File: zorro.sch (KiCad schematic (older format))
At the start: 76 parts, among them CN601 zorro_socket, CN602 zorro_socket, CN603 zorro_socket, CN604 zorro_socket, CN605 zorro_socket, CN606 Conn_01x04_Male, J1 Conn_01x03_Male, J2 Conn_01x03_Male, U606 74LS32

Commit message: Rename bus with correct syntax
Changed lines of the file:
@@
-EESchema Schematic File Version 4
+EESchema Schematic File Version 5
 LIBS:amiga2000-cache
 EELAYER 29 0
@@
 	14150 14500 14250 14600
 Text GLabel 4950 14600 0    50   Input ~ 0
-_SLAVE(1:5)
+_SLAVE[1..5]
 Wire Wire Line
 	7350 4200 9350 4200
@@
 	4650 5000 4150 5000
 Text GLabel 4150 5000 0    50   Input ~ 0
-BA(1:23)
+BA[1..23]
 Text Label 7400 9200 0    50   ~ 0
 _BR1
@@
 _BG5
 Text GLabel 4950 14450 0    50   Input ~ 0
-_EBR(1:5)
+_EBR[1..5]
 Text GLabel 4950 14300 0    50   Input ~ 0
-_EBG(1:5)
+_EBG[1..5]
 Wire Wire Line
 	7350 9600 7450 9600
@@
 	4600 9400 3950 9400
 Text GLabel 3950 9400 0    50   Input ~ 0
-BD(0:15)
+BD[0..15]
 $Comp
 L Device:C_Small C654
@@
 _IPL0
 Text GLabel 3050 6700 0    50   Input ~ 0
-_IPL(0:2)
+_IPL[0..2]
 $Comp
 L Device:R_Network09 RP601

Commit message: Some ERC things
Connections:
- net OVR renamed _OVR
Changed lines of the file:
@@
-EESchema Schematic File Version 5
+EESchema Schematic File Version 4
 LIBS:amiga2000-cache
 EELAYER 29 0
@@
 Connection ~ 15600 4800
 Text GLabel 6200 4900 0    50   Input ~ 0
-OVR
+_OVR
 Wire Wire Line
 	6200 4900 6300 4900

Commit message: Rename some bus things
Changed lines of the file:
@@
 _BG5
 Text GLabel 4950 14450 0    50   Input ~ 0
-_EBR[1..5]
+_BR[1..5]
 Text GLabel 4950 14300 0    50   Input ~ 0
-_EBG[1..5]
+_BG[1..5]
 Wire Wire Line
 	7350 9600 7450 9600

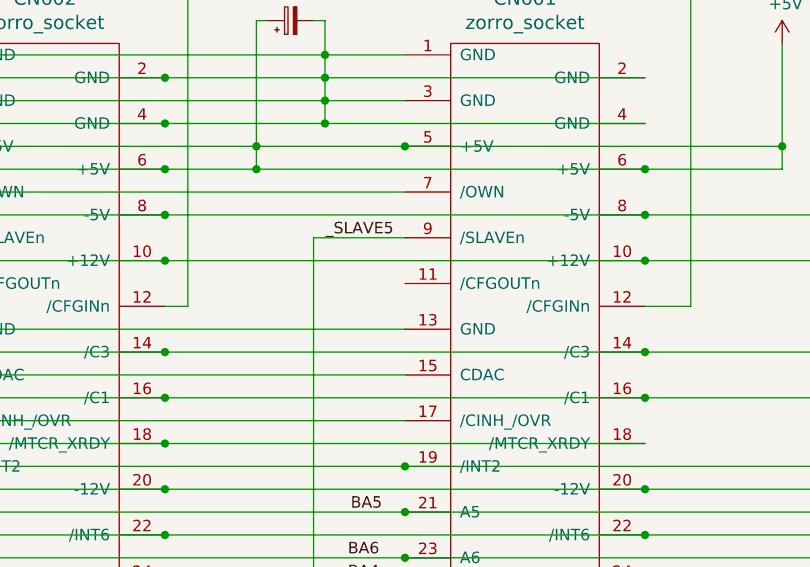
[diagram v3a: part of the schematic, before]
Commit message: Fix a bunch of DRC errors
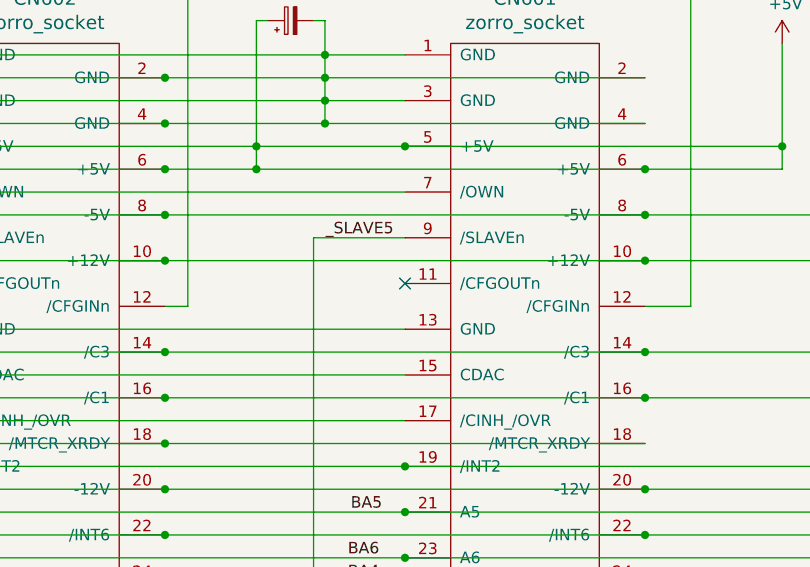
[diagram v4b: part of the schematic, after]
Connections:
- no-connect marks 0 -> 1
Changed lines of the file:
@@
 	0    -1   -1   0
 $EndComp
+NoConn ~ 14550 4300
 Wire Bus Line
 	3350 6700 3350 7050

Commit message: One more review
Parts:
- added RP600: 10k, Resistor_THT:R_Array_SIP8, symbol Device:R_Network07
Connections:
- net +5V: now also RP600.1 (common)
- net _BR1: now also RP600.6 (R5)
- net _BR2: now also RP600.5 (R4)
- net _BR3: now also RP600.4 (R3)
- net _BR4: now also RP600.3 (R2)
- net _BR5: now also RP600.2 (R1)
- no-connect marks 1 -> 3
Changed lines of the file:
@@
 $EndComp
 NoConn ~ 14550 4300
+$Comp
+L Device:R_Network07 RP600
+U 1 1 5D083E80
+P 17000 14950
+F 0 "RP600" V 16483 14950 50  0000 C CNN
+F 1 "10k" V 16574 14950 50  0000 C CNN
+F 2 "Resistor_THT:R_Array_SIP8" V 17475 14950 50  0001 C CNN
+F 3 "http://www.vishay.com/docs/31509/csc.pdf" H 17000 14950 50  0001 C CNN
+	1    17000 14950
+	0    1    1    0
+$EndComp
+Text Label 16550 14650 0    50   ~ 0
+_BR5
+Text Label 16550 14750 0    50   ~ 0
+_BR4
+Text Label 16550 14850 0    50   ~ 0
+_BR3
+Text Label 16550 14950 0    50   ~ 0
+_BR2
+Text Label 16550 15050 0    50   ~ 0
+_BR1
+$Comp
+L power:+5V #PWR0270
+U 1 1 5D186BDE
+P 17200 14650
+F 0 "#PWR0270" H 17200 14500 50  0001 C CNN
+F 1 "+5V" H 17215 14823 50  0000 C CNN
+F 2 "" H 17200 14650 50  0001 C CNN
+F 3 "" H 17200 14650 50  0001 C CNN
+	1    17200 14650
+	0    1    1    0
+$EndComp
+NoConn ~ 16800 15150
+NoConn ~ 16800 15250
+Entry Wire Line
+	16350 14550 16450 14650
+Entry Wire Line
+	16350 14650 16450 14750
+Entry Wire Line
+	16350 14750 16450 14850
+Entry Wire Line
+	16350 14850 16450 14950
+Entry Wire Line
+	16350 14950 16450 15050
+Wire Wire Line
+	16450 14650 16800 14650
+Wire Wire Line
+	16450 14750 16800 14750
+Wire Wire Line
+	16450 14850 16800 14850
+Wire Wire Line
+	16450 14950 16800 14950
+Wire Wire Line
+	16450 15050 16800 15050
 Wire Bus Line
 	3350 6700 3350 7050
-Wire Bus Line
-	4950 14450 16000 14450
 Wire Bus Line
 	4950 14600 14250 14600
@@
 	4950 14300 15850 14300
 Wire Bus Line
+	4950 14450 16350 14450
+Wire Bus Line
+	16350 14450 16350 14950
+Wire Bus Line
 	4600 9400 4600 11700

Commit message: Associate footprints with components
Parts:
- CN606: footprint (none) -> Connector_PinSocket_2.54mm:PinSocket_1x04_P2.54mm_Vertical
- J1, J2: footprint (none) -> Connector_PinSocket_2.54mm:PinSocket_1x03_P2.54mm_Vertical
- R311, R312, R601, R603, R604, R605, R901: footprint (none) -> Resistor_THT:R_Axial_DIN0207_L6.3mm_D2.5mm_P10.16mm_Horizontal
- U606: footprint (none) -> Package_DIP:DIP-14_W7.62mm_Socket
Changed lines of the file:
@@
 F 0 "CN604" H 8825 3447 60  0000 C CNN
 F 1 "zorro_socket" H 8825 3341 60  0000 C CNN
-F 2 "" H 8300 950 60  0000 C CNN
+F 2 "" H 8300 950 60  0001 C CNN
 F 3 "" H 8300 950 60  0000 C CNN
 	1    8800 3250
@@
 F 0 "CN603" H 11025 3447 60  0000 C CNN
 F 1 "zorro_socket" H 11025 3341 60  0000 C CNN
-F 2 "" H 10500 950 60  0000 C CNN
+F 2 "" H 10500 950 60  0001 C CNN
 F 3 "" H 10500 950 60  0000 C CNN
 	1    11000 3250
@@
 F 0 "CN602" H 12975 3447 60  0000 C CNN
 F 1 "zorro_socket" H 12975 3341 60  0000 C CNN
-F 2 "" H 12450 950 60  0000 C CNN
+F 2 "" H 12450 950 60  0001 C CNN
 F 3 "" H 12450 950 60  0000 C CNN
 	1    12950 3250
@@
 F 0 "CN601" H 15075 3447 60  0000 C CNN
 F 1 "zorro_socket" H 15075 3341 60  0000 C CNN
-F 2 "" H 14550 950 60  0000 C CNN
+F 2 "" H 14550 950 60  0001 C CNN
 F 3 "" H 14550 950 60  0000 C CNN
 	1    15050 3250
@@
 F 0 "CN605" H 6825 3447 60  0000 C CNN
 F 1 "zorro_socket" H 6825 3341 60  0000 C CNN
-F 2 "" H 6300 950 60  0000 C CNN
+F 2 "" H 6300 950 60  0001 C CNN
 F 3 "" H 6300 950 60  0000 C CNN
 	1    6800 3250
@@
 F 0 "R312" H 17320 3446 50  0000 L CNN
 F 1 "1k" H 17320 3355 50  0000 L CNN
-F 2 "" V 17180 3400 50  0001 C CNN
+F 2 "Resistor_THT:R_Axial_DIN0207_L6.3mm_D2.5mm_P10.16mm_Horizontal" V 17180 3400 50  0001 C CNN
 F 3 "~" H 17250 3400 50  0001 C CNN
 	1    17250 3400
@@
 F 0 "R311" H 17670 3446 50  0000 L CNN
 F 1 "1k" H 17670 3355 50  0000 L CNN
-F 2 "" V 17530 3400 50  0001 C CNN
+F 2 "Resistor_THT:R_Axial_DIN0207_L6.3mm_D2.5mm_P10.16mm_Horizontal" V 17530 3400 50  0001 C CNN
 F 3 "~" H 17600 3400 50  0001 C CNN
 	1    17600 3400
@@
 F 0 "U606" H 7800 2625 50  0000 C CNN
 F 1 "74LS32" H 7800 2534 50  0000 C CNN
-F 2 "" H 7800 2300 50  0001 C CNN
+F 2 "Package_DIP:DIP-14_W7.62mm_Socket" H 7800 2300 50  0001 C CNN
 F 3 "http://www.ti.com/lit/gpn/sn74LS32" H 7800 2300 50  0001 C CNN
 	4    7800 2300
@@
 F 0 "U606" H 9900 2725 50  0000 C CNN
 F 1 "74LS32" H 9900 2634 50  0000 C CNN
-F 2 "" H 9900 2400 50  0001 C CNN
+F 2 "Package_DIP:DIP-14_W7.62mm_Socket" H 9900 2400 50  0001 C CNN
 F 3 "http://www.ti.com/lit/gpn/sn74LS32" H 9900 2400 50  0001 C CNN
 	1    9900 2400
@@
 F 0 "U606" H 12100 2825 50  0000 C CNN
 F 1 "74LS32" H 12100 2734 50  0000 C CNN
-F 2 "" H 12100 2500 50  0001 C CNN
+F 2 "Package_DIP:DIP-14_W7.62mm_Socket" H 12100 2500 50  0001 C CNN
 F 3 "http://www.ti.com/lit/gpn/sn74LS32" H 12100 2500 50  0001 C CNN
 	2    12100 2500
@@
 F 0 "U606" H 14000 2925 50  0000 C CNN
 F 1 "74LS32" H 14000 2834 50  0000 C CNN
-F 2 "" H 14000 2600 50  0001 C CNN
+F 2 "Package_DIP:DIP-14_W7.62mm_Socket" H 14000 2600 50  0001 C CNN
 F 3 "http://www.ti.com/lit/gpn/sn74LS32" H 14000 2600 50  0001 C CNN
 	3    14000 2600
@@
 F 0 "J1" V 16800 13250 50  0000 R CNN
 F 1 "Conn_01x03_Male" V 16963 13012 50  0001 R CNN
-F 2 "" H 16900 13200 50  0001 C CNN
+F 2 "Connector_PinSocket_2.54mm:PinSocket_1x03_P2.54mm_Vertical" H 16900 13200 50  0001 C CNN
 F 3 "~" H 16900 13200 50  0001 C CNN
 	1    16900 13200
@@
 F 0 "J2" V 17150 13150 50  0000 R CNN
 F 1 "Conn_01x03_Male" V 17313 12912 50  0001 R CNN
-F 2 "" H 17250 13100 50  0001 C CNN
+F 2 "Connector_PinSocket_2.54mm:PinSocket_1x03_P2.54mm_Vertical" H 17250 13100 50  0001 C CNN
 F 3 "~" H 17250 13100 50  0001 C CNN
 	1    17250 13100
@@
 F 0 "U606" H 19730 14196 50  0000 L CNN
 F 1 "74LS32" H 19730 14105 50  0000 L CNN
-F 2 "" H 19500 14150 50  0001 C CNN
+F 2 "Package_DIP:DIP-14_W7.62mm_Socket" H 19500 14150 50  0001 C CNN
 F 3 "http://www.ti.com/lit/gpn/sn74LS32" H 19500 14150 50  0001 C CNN
 	5    19500 14150
@@
 F 0 "R603" H 18130 12854 50  0000 R CNN
 F 1 "1k" H 18130 12945 50  0000 R CNN
-F 2 "" V 18130 12900 50  0001 C CNN
+F 2 "Resistor_THT:R_Axial_DIN0207_L6.3mm_D2.5mm_P10.16mm_Horizontal" V 18130 12900 50  0001 C CNN
 F 3 "~" H 18200 12900 50  0001 C CNN
 	1    18200 12900
@@
 F 0 "R601" H 18580 12854 50  0000 R CNN
 F 1 "1k" H 18580 12945 50  0000 R CNN
-F 2 "" V 18580 12900 50  0001 C CNN
+F 2 "Resistor_THT:R_Axial_DIN0207_L6.3mm_D2.5mm_P10.16mm_Horizontal" V 18580 12900 50  0001 C CNN
 F 3 "~" H 18650 12900 50  0001 C CNN
 	1    18650 12900
@@
 F 0 "R605" H 21280 11104 50  0000 R CNN
 F 1 "1k" H 21280 11195 50  0000 R CNN
-F 2 "" V 21280 11150 50  0001 C CNN
+F 2 "Resistor_THT:R_Axial_DIN0207_L6.3mm_D2.5mm_P10.16mm_Horizontal" V 21280 11150 50  0001 C CNN
 F 3 "~" H 21350 11150 50  0001 C CNN
 	1    21350 11150
@@
 F 0 "R604" H 21730 11104 50  0000 R CNN
 F 1 "1k" H 21730 11195 50  0000 R CNN
-F 2 "" V 21730 11150 50  0001 C CNN
+F 2 "Resistor_THT:R_Axial_DIN0207_L6.3mm_D2.5mm_P10.16mm_Horizontal" V 21730 11150 50  0001 C CNN
 F 3 "~" H 21800 11150 50  0001 C CNN
 	1    21800 11150
@@
 F 0 "R901" H 21820 5296 50  0000 L CNN
 F 1 "Xk" H 21820 5205 50  0000 L CNN
-F 2 "" V 21680 5250 50  0001 C CNN
+F 2 "Resistor_THT:R_Axial_DIN0207_L6.3mm_D2.5mm_P10.16mm_Horizontal" V 21680 5250 50  0001 C CNN
 F 3 "~" H 21750 5250 50  0001 C CNN
 	1    21750 5250
@@
 F 0 "CN606" H 3922 6978 50  0000 R CNN
 F 1 "Conn_01x04_Male" H 4058 7240 50  0001 C CNN
-F 2 "" H 3950 7050 50  0001 C CNN
+F 2 "Connector_PinSocket_2.54mm:PinSocket_1x04_P2.54mm_Vertical" H 3950 7050 50  0001 C CNN
 F 3 "~" H 3950 7050 50  0001 C CNN
 	1    3950 7050
@@
 	4950 14300 15850 14300
 Wire Bus Line
-	4950 14450 16350 14450
-Wire Bus Line
 	16350 14450 16350 14950
 Wire Bus Line
+	4950 14450 16350 14450
+Wire Bus Line
 	4600 9400 4600 11700

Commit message: Associate more components
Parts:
- C416, C417, C418, C419: footprint (none) -> Capacitor_THT:C_Axial_L12.0mm_D7.5mm_P20.00mm_Horizontal
- C902, C917: value XXpF -> empty
- R901: value Xk -> empty
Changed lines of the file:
@@
 F 0 "C416" V 7925 3150 50  0000 C CNN
 F 1 "220uF 16V" V 7834 3150 50  0000 C CNN
-F 2 "" H 7700 3150 50  0001 C CNN
+F 2 "Capacitor_THT:C_Axial_L12.0mm_D7.5mm_P20.00mm_Horizontal" H 7700 3150 50  0001 C CNN
 F 3 "~" H 7700 3150 50  0001 C CNN
 	1    7700 3150
@@
 F 0 "C417" V 10025 3150 50  0000 C CNN
 F 1 "220uF 16V" V 9934 3150 50  0000 C CNN
-F 2 "" H 9800 3150 50  0001 C CNN
+F 2 "Capacitor_THT:C_Axial_L12.0mm_D7.5mm_P20.00mm_Horizontal" H 9800 3150 50  0001 C CNN
 F 3 "~" H 9800 3150 50  0001 C CNN
 	1    9800 3150
@@
 F 0 "C418" V 12125 3150 50  0000 C CNN
 F 1 "220uF 16V" V 12034 3150 50  0000 C CNN
-F 2 "" H 11900 3150 50  0001 C CNN
+F 2 "Capacitor_THT:C_Axial_L12.0mm_D7.5mm_P20.00mm_Horizontal" H 11900 3150 50  0001 C CNN
 F 3 "~" H 11900 3150 50  0001 C CNN
 	1    11900 3150
@@
 F 0 "C419" V 14275 3150 50  0000 C CNN
 F 1 "220uF 16V" V 14184 3150 50  0000 C CNN
-F 2 "" H 14050 3150 50  0001 C CNN
+F 2 "Capacitor_THT:C_Axial_L12.0mm_D7.5mm_P20.00mm_Horizontal" H 14050 3150 50  0001 C CNN
 F 3 "~" H 14050 3150 50  0001 C CNN
 	1    14050 3150
@@
 P 21750 5250
 F 0 "R901" H 21820 5296 50  0000 L CNN
-F 1 "Xk" H 21820 5205 50  0000 L CNN
+F 1 "empty" H 21820 5205 50  0000 L CNN
 F 2 "Resistor_THT:R_Axial_DIN0207_L6.3mm_D2.5mm_P10.16mm_Horizontal" V 21680 5250 50  0001 C CNN
 F 3 "~" H 21750 5250 50  0001 C CNN
@@
 P 22150 5250
 F 0 "C917" H 22265 5296 50  0000 L CNN
-F 1 "XXpF" H 22265 5205 50  0000 L CNN
+F 1 "empty" H 22265 5205 50  0000 L CNN
 F 2 "" H 22188 5100 50  0001 C CNN
 F 3 "~" H 22150 5250 50  0001 C CNN
@@
 P 22550 5250
 F 0 "C902" H 22665 5296 50  0000 L CNN
-F 1 "XXpF" H 22665 5205 50  0000 L CNN
+F 1 "empty" H 22665 5205 50  0000 L CNN
 F 2 "" H 22588 5100 50  0001 C CNN
 F 3 "~" H 22550 5250 50  0001 C CNN
